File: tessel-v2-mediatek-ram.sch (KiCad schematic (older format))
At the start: 0 parts

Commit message: moved RAM
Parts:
- added U?: MT7620N, symbol MT7620N
- added U?: W9751G6KB-25, symbol W9751G6KB-25
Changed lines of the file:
@@
 Comment4 ""
 $EndDescr
+$Comp
+L MT7620N U?
+U 2 1 548CE37F
+P 4650 5650
+AR Path="/548C90C9/548CE37F" Ref="U?"  Part="2"
+AR Path="/548C90C9/548CC02E/548CE37F" Ref="U?"  Part="2"
+F 0 "U?" H 3850 6750 60  0000 C CNN
+F 1 "MT7620N" H 3950 6650 60  0000 C CNN
+F 2 "" H 3100 6150 60  0000 C CNN
+F 3 "" H 3100 6150 60  0000 C CNN
+	2    4650 5650
+	1    0    0    -1
+$EndComp
+Text Label 4400 4550 1    60   ~ 0
+DDR_CKE
+Text Label 4500 4550 1    60   ~ 0
+DDR_CS
+Text Label 4600 4550 1    60   ~ 0
+DDR_CAS
+Text Label 4700 4550 1    60   ~ 0
+DDR_RAS
+Text Label 4800 4550 1    60   ~ 0
+DDR_WE
+Wire Wire Line
+	4400 3900 4400 4550
+Wire Wire Line
+	4500 3900 4500 4550
+Wire Wire Line
+	4600 3900 4600 4550
+Wire Wire Line
+	4700 3900 4700 4550
+Wire Wire Line
+	4800 3900 4800 4550
+Entry Wire Line
+	4300 3800 4400 3900
+Entry Wire Line
+	4400 3800 4500 3900
+Entry Wire Line
+	4500 3800 4600 3900
+Entry Wire Line
+	4600 3800 4700 3900
+Entry Wire Line
+	4700 3800 4800 3900
+Wire Bus Line
+	4700 3800 4200 3800
+Wire Wire Line
+	4400 3950 5050 3950
+Connection ~ 4400 3950
+Text GLabel 5050 3950 2    60   Input ~ 0
+DDR_CKE
+Wire Wire Line
+	4500 4100 5050 4100
+Connection ~ 4500 4100
+Wire Wire Line
+	4600 4250 5050 4250
+Connection ~ 4600 4250
+Wire Wire Line
+	4700 4400 5050 4400
+Connection ~ 4700 4400
+Wire Wire Line
+	4800 4550 5050 4550
+Text GLabel 5050 4100 2    60   Input ~ 0
+DDR_CS
+Text GLabel 5050 4250 2    60   Input ~ 0
+DDR_CAS
+Text GLabel 5050 4400 2    60   Input ~ 0
+DDR_RAS
+Text GLabel 5050 4550 2    60   Input ~ 0
+DDR_WE
+Text HLabel 4200 3800 0    60   Input ~ 0
+DDR
+$Comp
+L W9751G6KB-25 U?
+U 1 1 548CFEFF
+P 10150 5750
+F 0 "U?" H 9000 7500 60  0000 C CNN
+F 1 "W9751G6KB-25" H 10150 5750 60  0000 C CNN
+F 2 "" H 8550 6150 60  0000 C CNN
+F 3 "" H 8550 6150 60  0000 C CNN
+	1    10150 5750
+	1    0    0    -1
+$EndComp
 $EndSCHEMATC

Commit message: connecting ram
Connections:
- net at U?.104 (DDR_MA3): now also U?.N2 (A3)
- net at U?.105 (DDR_MA2): now also U?.M7 (A2)
- net at U?.106 (DDR_MA0): now also U?.M8 (A0)
- net at U?.17 (DDR_MA4): now also U?.N8 (A4)
- net at U?.19 (DDR_MA7): now also U?.P2 (A7)
- net at U?.20 (DDR_MA8): now also U?.P8 (A8)
- net at U?.21 (DDR_MA11): now also U?.P7 (A11)
- net at U?.30 (DDR_MA1): now also U?.M3 (A1)
- net at U?.31 (DDR_MA10): now also U?.M2 (A10/AP)
- net at U?.92 (DDR_MA5): now also U?.N3 (A5)
- net at U?.94 (DDR_MA6): now also U?.N7 (A6)
- net at U?.96 (DDR_MA9): now also U?.P3 (A9)
- net at U?.97 (DDR_MA12): now also U?.R2 (A12)
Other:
- moved on the sheet: U?B
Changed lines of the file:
@@
 L MT7620N U?
 U 2 1 548CE37F
-P 4650 5650
+P 7300 6100
 AR Path="/548C90C9/548CE37F" Ref="U?"  Part="2"
 AR Path="/548C90C9/548CC02E/548CE37F" Ref="U?"  Part="2"
-F 0 "U?" H 3850 6750 60  0000 C CNN
-F 1 "MT7620N" H 3950 6650 60  0000 C CNN
-F 2 "" H 3100 6150 60  0000 C CNN
-F 3 "" H 3100 6150 60  0000 C CNN
-	2    4650 5650
+F 0 "U?" H 6500 7200 60  0000 C CNN
+F 1 "MT7620N" H 6600 7100 60  0000 C CNN
+F 2 "" H 5750 6600 60  0000 C CNN
+F 3 "" H 5750 6600 60  0000 C CNN
+	2    7300 6100
 	1    0    0    -1
 $EndComp
@@
 Text Label 4800 4550 1    60   ~ 0
 DDR_WE
-Wire Wire Line
-	4400 3900 4400 4550
-Wire Wire Line
-	4500 3900 4500 4550
-Wire Wire Line
-	4600 3900 4600 4550
-Wire Wire Line
-	4700 3900 4700 4550
-Wire Wire Line
-	4800 3900 4800 4550
 Entry Wire Line
 	4300 3800 4400 3900
@@
 Entry Wire Line
 	4700 3800 4800 3900
-Wire Bus Line
-	4700 3800 4200 3800
-Wire Wire Line
-	4400 3950 5050 3950
-Connection ~ 4400 3950
 Text GLabel 5050 3950 2    60   Input ~ 0
 DDR_CKE
-Wire Wire Line
-	4500 4100 5050 4100
-Connection ~ 4500 4100
-Wire Wire Line
-	4600 4250 5050 4250
-Connection ~ 4600 4250
-Wire Wire Line
-	4700 4400 5050 4400
-Connection ~ 4700 4400
-Wire Wire Line
-	4800 4550 5050 4550
 Text GLabel 5050 4100 2    60   Input ~ 0
 DDR_CS
@@
 	1    0    0    -1
 $EndComp
+Wire Wire Line
+	4400 3900 4400 4550
+Wire Wire Line
+	4500 3900 4500 4550
+Wire Wire Line
+	4600 3900 4600 4550
+Wire Wire Line
+	4700 3900 4700 4550
+Wire Wire Line
+	4800 3900 4800 4550
+Wire Bus Line
+	4700 3800 4200 3800
+Wire Wire Line
+	4400 3950 5050 3950
+Connection ~ 4400 3950
+Wire Wire Line
+	4500 4100 5050 4100
+Connection ~ 4500 4100
+Wire Wire Line
+	4600 4250 5050 4250
+Connection ~ 4600 4250
+Wire Wire Line
+	4700 4400 5050 4400
+Connection ~ 4700 4400
+Wire Wire Line
+	4800 4550 5050 4550
+Wire Wire Line
+	7850 5250 8750 5250
+Wire Wire Line
+	8750 5350 7850 5350
+Wire Wire Line
+	7850 5450 8750 5450
+Wire Wire Line
+	7850 5550 8750 5550
+Wire Wire Line
+	7850 5650 8750 5650
+Wire Wire Line
+	7850 5750 8750 5750
+Wire Wire Line
+	7850 5850 8750 5850
+Wire Wire Line
+	7850 5950 8750 5950
+Wire Wire Line
+	8750 6050 7850 6050
+Wire Wire Line
+	7850 6150 8750 6150
+Wire Wire Line
+	7850 6250 8750 6250
+Wire Wire Line
+	7850 6350 8750 6350
+Wire Wire Line
+	7850 6450 8750 6450
 $EndSCHEMATC

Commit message: added ddr
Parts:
- added C?: 10nF, symbol C
- added C? (x2): 5pF, symbol C
- added C? (x7): 0.1uF, symbol C
- added R?: 120, symbol R
- added R? (x2): 22, symbol R
- added R? (x2): 5k, symbol R
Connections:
- net labels added: +1V8, A0, A1, A10, A11, A12, A2, A3, A4, A5, A6, A7, A8, A9, BA0, BA1, CAS_N, CKE, CLK, CLK_N, CS_N, DDR_VREF, DQ0, DQ1, DQ10, DQ11, DQ12, DQ13, DQ14, DQ15, DQ2, DQ3, DQ4, DQ5, DQ6, DQ7, DQ8, DQ9, DQM0, DQM1, DQS0, DQS1, GND, MCK_N, MCK_P, ODT, RAS_N, WE_N
- net labels removed: DDR, DDR_CAS, DDR_CKE, DDR_CS, DDR_RAS, DDR_WE
- wire segments 23 -> 156

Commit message: changed 5k to 4.7k
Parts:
- R? (x2): value 5k -> 4.7k
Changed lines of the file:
@@
 P 9400 8350
 F 0 "R?" V 9480 8350 40  0000 C CNN
-F 1 "5k" V 9407 8351 40  0000 C CNN
+F 1 "4.7k" V 9407 8351 40  0000 C CNN
 F 2 "" V 9330 8350 30  0000 C CNN
 F 3 "" H 9400 8350 30  0000 C CNN
@@
 P 9750 8600
 F 0 "R?" V 9830 8600 40  0000 C CNN
-F 1 "5k" V 9757 8601 40  0000 C CNN
+F 1 "4.7k" V 9757 8601 40  0000 C CNN
 F 2 "" V 9680 8600 30  0000 C CNN
 F 3 "" H 9750 8600 30  0000 C CNN

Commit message: swapped in power labels
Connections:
- net labels added: +1.8V
- net labels removed: +1V8
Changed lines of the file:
@@
 Text Label 6300 4250 0    60   ~ 0
 MCK_N
-$Comp
-L +1V8 #PWR?
-U 1 1 548D62C2
-P 10000 3400
-F 0 "#PWR?" H 10000 3250 60  0001 C CNN
-F 1 "+1V8" H 10000 3540 60  0000 C CNN
-F 2 "" H 10000 3400 60  0000 C CNN
-F 3 "" H 10000 3400 60  0000 C CNN
-	1    10000 3400
-	1    0    0    -1
-$EndComp
 Wire Wire Line
 	7850 5250 8750 5250
@@
 	9150 8100 9150 8350
 $Comp
-L +1V8 #PWR?
-U 1 1 548D784F
-P 9150 8100
-F 0 "#PWR?" H 9150 7950 60  0001 C CNN
-F 1 "+1V8" H 9150 8240 60  0000 C CNN
-F 2 "" H 9150 8100 60  0000 C CNN
-F 3 "" H 9150 8100 60  0000 C CNN
-	1    9150 8100
-	1    0    0    -1
-$EndComp
-$Comp
 L C C?
 U 1 1 548D79BD
@@
 Connection ~ 13650 5850
 $Comp
-L +1V8 #PWR?
-U 1 1 548D886F
-P 13900 5150
-F 0 "#PWR?" H 13900 5000 60  0001 C CNN
-F 1 "+1V8" H 13900 5290 60  0000 C CNN
-F 2 "" H 13900 5150 60  0000 C CNN
-F 3 "" H 13900 5150 60  0000 C CNN
-	1    13900 5150
-	1    0    0    -1
-$EndComp
-$Comp
 L GND #PWR?
 U 1 1 548D88C7
@@
 	1    0    0    -1
 $EndComp
+$Comp
+L +1.8V #PWR?
+U 1 1 5490BE7F
+P 10000 3400
+F 0 "#PWR?" H 10000 3540 20  0001 C CNN
+F 1 "+1.8V" H 10000 3510 30  0000 C CNN
+F 2 "" H 10000 3400 60  0000 C CNN
+F 3 "" H 10000 3400 60  0000 C CNN
+	1    10000 3400
+	1    0    0    -1
+$EndComp
+$Comp
+L +1.8V #PWR?
+U 1 1 5490C3F5
+P 13900 5150
+F 0 "#PWR?" H 13900 5290 20  0001 C CNN
+F 1 "+1.8V" H 13900 5260 30  0000 C CNN
+F 2 "" H 13900 5150 60  0000 C CNN
+F 3 "" H 13900 5150 60  0000 C CNN
+	1    13900 5150
+	1    0    0    -1
+$EndComp
+$Comp
+L +1.8V #PWR?
+U 1 1 5490C6A2
+P 9150 8100
+F 0 "#PWR?" H 9150 8240 20  0001 C CNN
+F 1 "+1.8V" H 9150 8210 30  0000 C CNN
+F 2 "" H 9150 8100 60  0000 C CNN
+F 3 "" H 9150 8100 60  0000 C CNN
+	1    9150 8100
+	1    0    0    -1
+$EndComp

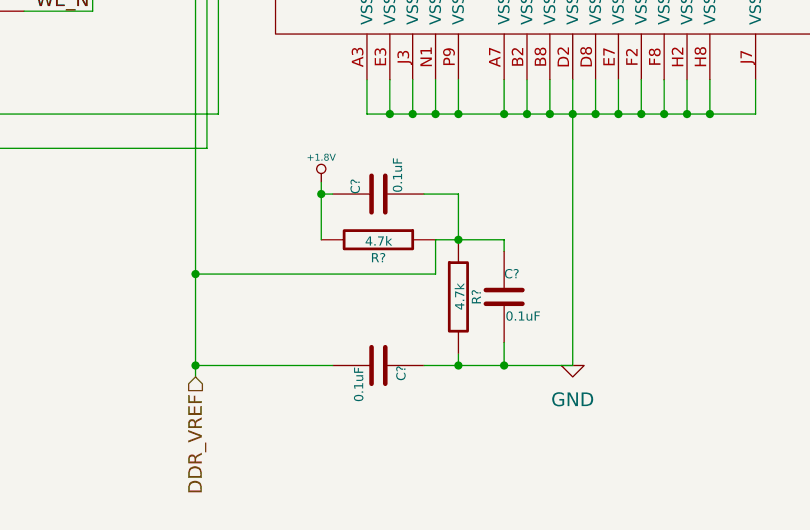
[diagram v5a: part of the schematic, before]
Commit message: cleaning up ram, rf, and mediatek power
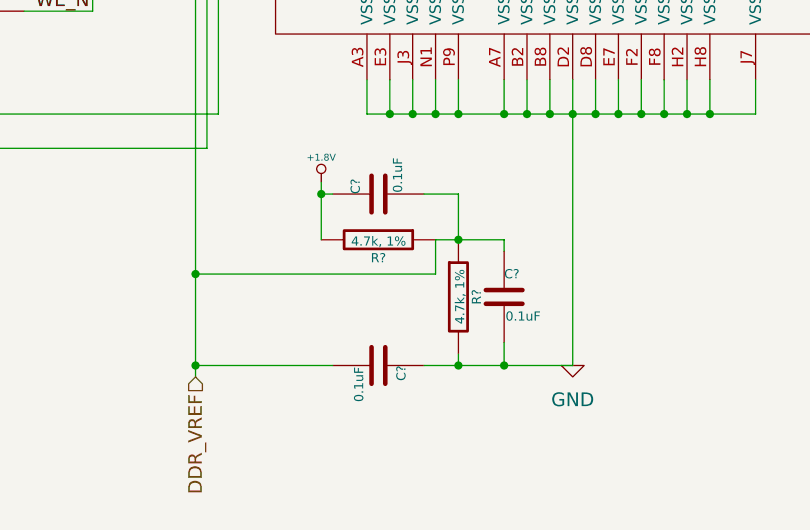
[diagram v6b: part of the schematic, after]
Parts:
- R? (x2): value 4.7k -> 4.7k, 1%
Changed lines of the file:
@@
 P 9400 8350
 F 0 "R?" V 9480 8350 40  0000 C CNN
-F 1 "4.7k" V 9407 8351 40  0000 C CNN
+F 1 "4.7k, 1%" V 9407 8351 40  0000 C CNN
 F 2 "" V 9330 8350 30  0000 C CNN
 F 3 "" H 9400 8350 30  0000 C CNN
@@
 P 9750 8600
 F 0 "R?" V 9830 8600 40  0000 C CNN
-F 1 "4.7k" V 9757 8601 40  0000 C CNN
+F 1 "4.7k, 1%" V 9757 8601 40  0000 C CNN
 F 2 "" V 9680 8600 30  0000 C CNN
 F 3 "" H 9750 8600 30  0000 C CNN

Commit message: annotated
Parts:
- gave numbers to parts that had none: 17
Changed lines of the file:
@@
 P 7300 6100
 AR Path="/548C90C9/548CE37F" Ref="U?"  Part="2"
-AR Path="/548C90C9/548CC02E/548CE37F" Ref="U?"  Part="2"
-F 0 "U?" H 6500 7200 60  0000 C CNN
+AR Path="/548C90C9/548CC02E/548CE37F" Ref="U201"  Part="2"
+F 0 "U201" H 6500 7200 60  0000 C CNN
 F 1 "MT7620N" H 6600 7100 60  0000 C CNN
 F 2 "" H 5750 6600 60  0000 C CNN
@@
 $EndComp
 $Comp
-L W9751G6KB-25 U?
+L W9751G6KB-25 U301
 U 1 1 548CFEFF
 P 10150 5750
-F 0 "U?" H 9000 7500 60  0000 C CNN
+F 0 "U301" H 9000 7500 60  0000 C CNN
 F 1 "W9751G6KB-25" H 10150 5750 60  0000 C CNN
 F 2 "" H 8550 6150 60  0000 C CNN
@@
 DQS0
 $Comp
-L GND #PWR?
+L GND #PWR304
 U 1 1 548D31D5
 P 10250 8900
-F 0 "#PWR?" H 10250 8650 60  0001 C CNN
+F 0 "#PWR304" H 10250 8650 60  0001 C CNN
 F 1 "GND" H 10250 8750 60  0000 C CNN
 F 2 "" H 10250 8900 60  0000 C CNN
@@
 DDR_VREF
 $Comp
-L C C?
+L C C306
 U 1 1 548D3587
 P 13400 5600
-F 0 "C?" H 13400 5700 40  0000 L CNN
+F 0 "C306" H 13400 5700 40  0000 L CNN
 F 1 "10nF" H 13406 5515 40  0000 L CNN
 F 2 "" H 13438 5450 30  0000 C CNN
@@
 $EndComp
 $Comp
-L R R?
+L R R303
 U 1 1 548D36D9
 P 7650 4300
-F 0 "R?" V 7730 4300 40  0000 C CNN
+F 0 "R303" V 7730 4300 40  0000 C CNN
 F 1 "120" V 7657 4301 40  0000 C CNN
 F 2 "" V 7580 4300 30  0000 C CNN
@@
 CLK_N
 $Comp
-L R R?
+L R R301
 U 1 1 548D3CA8
 P 6850 4050
-F 0 "R?" V 6930 4050 40  0000 C CNN
+F 0 "R301" V 6930 4050 40  0000 C CNN
 F 1 "22" V 6857 4051 40  0000 C CNN
 F 2 "" V 6780 4050 30  0000 C CNN
@@
 $EndComp
 $Comp
-L R R?
+L R R302
 U 1 1 548D3CD9
 P 6850 4250
-F 0 "R?" V 6930 4250 40  0000 C CNN
+F 0 "R302" V 6930 4250 40  0000 C CNN
 F 1 "22" V 6857 4251 40  0000 C CNN
 F 2 "" V 6780 4250 30  0000 C CNN
@@
 $EndComp
 $Comp
-L C C?
+L C C302
 U 1 1 548D48B9
 P 7400 4550
-F 0 "C?" H 7400 4650 40  0000 L CNN
+F 0 "C302" H 7400 4650 40  0000 L CNN
 F 1 "5pF" H 7406 4465 40  0000 L CNN
 F 2 "" H 7438 4400 30  0000 C CNN
@@
 $EndComp
 $Comp
-L C C?
+L C C301
 U 1 1 548D4B3C
 P 7200 4550
-F 0 "C?" H 7200 4650 40  0000 L CNN
+F 0 "C301" H 7200 4650 40  0000 L CNN
 F 1 "5pF" H 7206 4465 40  0000 L CNN
 F 2 "" H 7238 4400 30  0000 C CNN
@@
 $EndComp
 $Comp
-L GND #PWR?
+L GND #PWR301
 U 1 1 548D4FEE
 P 7300 4850
-F 0 "#PWR?" H 7300 4600 60  0001 C CNN
+F 0 "#PWR301" H 7300 4600 60  0001 C CNN
 F 1 "GND" H 7300 4700 60  0000 C CNN
 F 2 "" H 7300 4850 60  0000 C CNN
@@
 Connection ~ 7650 4650
 $Comp
-L C C?
+L C C304
 U 1 1 548D6B14
 P 9400 8900
-F 0 "C?" H 9400 9000 40  0000 L CNN
+F 0 "C304" H 9400 9000 40  0000 L CNN
 F 1 "0.1uF" H 9406 8815 40  0000 L CNN
 F 2 "" H 9438 8750 30  0000 C CNN
@@
 $EndComp
 $Comp
-L R R?
+L R R304
 U 1 1 548D6FE8
 P 9400 8350
-F 0 "R?" V 9480 8350 40  0000 C CNN
+F 0 "R304" V 9480 8350 40  0000 C CNN
 F 1 "4.7k, 1%" V 9407 8351 40  0000 C CNN
 F 2 "" V 9330 8350 30  0000 C CNN
@@
 $EndComp
 $Comp
-L R R?
+L R R305
 U 1 1 548D71F3
 P 9750 8600
-F 0 "R?" V 9830 8600 40  0000 C CNN
+F 0 "R305" V 9830 8600 40  0000 C CNN
 F 1 "4.7k, 1%" V 9757 8601 40  0000 C CNN
 F 2 "" V 9680 8600 30  0000 C CNN
@@
 	9150 8100 9150 8350
 $Comp
-L C C?
+L C C303
 U 1 1 548D79BD
 P 9400 8150
-F 0 "C?" H 9400 8250 40  0000 L CNN
+F 0 "C303" H 9400 8250 40  0000 L CNN
 F 1 "0.1uF" H 9406 8065 40  0000 L CNN
 F 2 "" H 9438 8000 30  0000 C CNN
@@
 $EndComp
 $Comp
-L C C?
+L C C305
 U 1 1 548D79FD
 P 9950 8600
-F 0 "C?" H 9950 8700 40  0000 L CNN
+F 0 "C305" H 9950 8700 40  0000 L CNN
 F 1 "0.1uF" H 9956 8515 40  0000 L CNN
 F 2 "" H 9988 8450 30  0000 C CNN
@@
 	9750 8150 9750 8350
 $Comp
-L C C?
+L C C307
 U 1 1 548D7FDE
 P 13650 5600
-F 0 "C?" H 13650 5700 40  0000 L CNN
+F 0 "C307" H 13650 5700 40  0000 L CNN
 F 1 "0.1uF" H 13656 5515 40  0000 L CNN
 F 2 "" H 13688 5450 30  0000 C CNN
@@
 $EndComp
 $Comp
-L C C?
+L C C308
 U 1 1 548D8010
 P 13900 5600
-F 0 "C?" H 13900 5700 40  0000 L CNN
+F 0 "C308" H 13900 5700 40  0000 L CNN
 F 1 "0.1uF" H 13906 5515 40  0000 L CNN
 F 2 "" H 13938 5450 30  0000 C CNN
@@
 $EndComp
 $Comp
-L C C?
+L C C309
 U 1 1 548D803B
 P 14150 5600
-F 0 "C?" H 14150 5700 40  0000 L CNN
+F 0 "C309" H 14150 5700 40  0000 L CNN
 F 1 "0.1uF" H 14156 5515 40  0000 L CNN
 F 2 "" H 14188 5450 30  0000 C CNN
@@
 $EndComp
 $Comp
-L C C?
+L C C310
 U 1 1 548D8069
 P 14400 5600
-F 0 "C?" H 14400 5700 40  0000 L CNN
+F 0 "C310" H 14400 5700 40  0000 L CNN
 F 1 "0.1uF" H 14406 5515 40  0000 L CNN
 F 2 "" H 14438 5450 30  0000 C CNN
@@
 Connection ~ 13650 5850
 $Comp
-L GND #PWR?
+L GND #PWR306
 U 1 1 548D88C7
 P 13900 6050
-F 0 "#PWR?" H 13900 5800 60  0001 C CNN
+F 0 "#PWR306" H 13900 5800 60  0001 C CNN
 F 1 "GND" H 13900 5900 60  0000 C CNN
 F 2 "" H 13900 6050 60  0000 C CNN
@@
 $EndComp
 $Comp
-L +1.8V #PWR?
+L +1.8V #PWR303
 U 1 1 5490BE7F
 P 10000 3400
-F 0 "#PWR?" H 10000 3540 20  0001 C CNN
+F 0 "#PWR303" H 10000 3540 20  0001 C CNN
 F 1 "+1.8V" H 10000 3510 30  0000 C CNN
 F 2 "" H 10000 3400 60  0000 C CNN
@@
 $EndComp
 $Comp
-L +1.8V #PWR?
+L +1.8V #PWR305
 U 1 1 5490C3F5
 P 13900 5150
-F 0 "#PWR?" H 13900 5290 20  0001 C CNN
+F 0 "#PWR305" H 13900 5290 20  0001 C CNN
 F 1 "+1.8V" H 13900 5260 30  0000 C CNN
 F 2 "" H 13900 5150 60  0000 C CNN
@@
 $EndComp
 $Comp
-L +1.8V #PWR?
+L +1.8V #PWR302
 U 1 1 5490C6A2
 P 9150 8100
-F 0 "#PWR?" H 9150 8240 20  0001 C CNN
+F 0 "#PWR302" H 9150 8240 20  0001 C CNN
 F 1 "+1.8V" H 9150 8210 30  0000 C CNN
 F 2 "" H 9150 8100 60  0000 C CNN

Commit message: give nF some love
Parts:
- C303, C304, C305, C307, C308, C309, C310: value 0.1uF -> 100nF
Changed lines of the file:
@@
 P 9400 8900
 F 0 "C304" H 9400 9000 40  0000 L CNN
-F 1 "0.1uF" H 9406 8815 40  0000 L CNN
+F 1 "100nF" H 9406 8815 40  0000 L CNN
 F 2 "" H 9438 8750 30  0000 C CNN
 F 3 "" H 9400 8900 60  0000 C CNN
@@
 P 9400 8150
 F 0 "C303" H 9400 8250 40  0000 L CNN
-F 1 "0.1uF" H 9406 8065 40  0000 L CNN
+F 1 "100nF" H 9406 8065 40  0000 L CNN
 F 2 "" H 9438 8000 30  0000 C CNN
 F 3 "" H 9400 8150 60  0000 C CNN
@@
 P 9950 8600
 F 0 "C305" H 9950 8700 40  0000 L CNN
-F 1 "0.1uF" H 9956 8515 40  0000 L CNN
+F 1 "100nF" H 9956 8515 40  0000 L CNN
 F 2 "" H 9988 8450 30  0000 C CNN
 F 3 "" H 9950 8600 60  0000 C CNN
@@
 P 13650 5600
 F 0 "C307" H 13650 5700 40  0000 L CNN
-F 1 "0.1uF" H 13656 5515 40  0000 L CNN
+F 1 "100nF" H 13656 5515 40  0000 L CNN
 F 2 "" H 13688 5450 30  0000 C CNN
 F 3 "" H 13650 5600 60  0000 C CNN
@@
 P 13900 5600
 F 0 "C308" H 13900 5700 40  0000 L CNN
-F 1 "0.1uF" H 13906 5515 40  0000 L CNN
+F 1 "100nF" H 13906 5515 40  0000 L CNN
 F 2 "" H 13938 5450 30  0000 C CNN
 F 3 "" H 13900 5600 60  0000 C CNN
@@
 P 14150 5600
 F 0 "C309" H 14150 5700 40  0000 L CNN
-F 1 "0.1uF" H 14156 5515 40  0000 L CNN
+F 1 "100nF" H 14156 5515 40  0000 L CNN
 F 2 "" H 14188 5450 30  0000 C CNN
 F 3 "" H 14150 5600 60  0000 C CNN
@@
 P 14400 5600
 F 0 "C310" H 14400 5700 40  0000 L CNN
-F 1 "0.1uF" H 14406 5515 40  0000 L CNN
+F 1 "100nF" H 14406 5515 40  0000 L CNN
 F 2 "" H 14438 5450 30  0000 C CNN
 F 3 "" H 14400 5600 60  0000 C CNN
